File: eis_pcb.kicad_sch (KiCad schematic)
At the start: 69 parts, among them J1 527451897, J12 104031-0811, J2 GSB1C41110SSHR, J4 541020164, P1 V.BATT, P2 GND.BATT, Q3 IRLML6344TRPBF, SW1 SWT0210-045026GSA, SW2 SWT0210-045026GSA_REVA, U1 ESP32-S3-WROOM-1-N8R8, U2 AD5941BCPZ, U3 TMUX1109RSVR, U4 LSM6DSVTR, U5 BQ24075RGT, U6 NCP186AMX330TAG

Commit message: complete noise suppression, begin layout
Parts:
- removed SW1: SWT0210-045026GSA, SWT0210_045026GSA:SW_SWT0210-045026GSA_REVA, symbol SWT0210-045026GSA_REVA:SWT0210-045026GSA_REVA
- removed SW2: SWT0210-045026GSA_REVA, SWT0210_045026GSA:SW_SWT0210-045026GSA_REVA, symbol SWT0210-045026GSA_REVA:SWT0210-045026GSA_REVA
- added C15, C16, C36, C39, C41: 1u, Capacitor_SMD:C_0603_1608Metric, symbol Device:C_Small
- added C17, C32, C33, C35, C37, C38, C40: 100n, Capacitor_SMD:C_0402_1005Metric, symbol Device:C_Small
- added C34: 10u, Capacitor_SMD:C_0603_1608Metric, symbol Device:C_Small
- added FB1: 600R@100MHz, Diode_SMD:D_0805_2012Metric, symbol Device:FerriteBead_Small
- added R6, R7: 2.2R, Resistor_SMD:R_0402_1005Metric, symbol Device:R_Small_US
- added S1: PWR, SLW_864587_2A_RA_N_D:SW_SLW-864587-2A-RA-N-D, symbol SLW-864587-2A-RA-N-D:SLW-864587-2A-RA-N-D
- added SW1: RST, R_667995:R-667995_MIT, symbol Switch:SW_SPST
- added SW2: BOOT, R_667995:R-667995_MIT, symbol Switch:SW_SPST
- C11, C20, C5: footprint Capacitor_SMD:C_0402_1005Metric -> Capacitor_SMD:C_0603_1608Metric
- C12, C21, C26: value 0.1u -> 100n
- C13: value 0.1u -> 100n; footprint (none) -> Capacitor_SMD:C_0402_1005Metric
- C14: footprint (none) -> Capacitor_SMD:C_0402_1005Metric
- C18: value 10u -> 100n
- C19, C23: value 1u -> 100n
- C2: value 100n -> 1u; footprint Capacitor_SMD:C_0402_1005Metric -> Capacitor_SMD:C_0603_1608Metric
- C24: value 1u -> 22u; footprint Capacitor_SMD:C_0402_1005Metric -> Capacitor_SMD:C_0603_1608Metric
- C3: value 100n -> 10u; footprint Capacitor_SMD:C_0402_1005Metric -> Capacitor_SMD:C_0603_1608Metric
- C31: value 10u -> 100n; footprint Capacitor_SMD:C_0603_1608Metric -> Capacitor_SMD:C_0402_1005Metric
- J1: footprint CON_527451897_MOL -> 527451897:CON_527451897_MOL
- P1, P2: footprint (none) -> TestPoint:TestPoint_THTPad_D2.5mm_Drill1.2mm
- R3, R4, R5: footprint (none) -> Resistor_SMD:R_0402_1005Metric
- U1: footprint ESP32-S3-WROOM-1-N8R8:XCVR_ESP32S3WROOM1N8R8 -> RF_Module:ESP32-S3-WROOM-1
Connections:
- net +3V3: now also C16.1, C36.1, C37.1, C38.1, C40.1, C41.1, FB1.1, R7.2; no longer C1.1, C13.1, C2.1, C3.1, U2.30 (AVDD), U2.41 (AVDD), U2.6 (DVDD), U3.12 (VDD)
- net +5V: now also C33.2, C34.2
- net +VSYS: now also C35.1, S1.3; no longer C29.1, U5.10 (OUT), U5.11 (OUT)
- net BOOT: now also SW2.A
- net CS.AFE: no longer U1.31 (IO38)
- net CS.SCREEN: now also U1.18 (IO10); no longer R27.1, U1.32 (IO39)
- net CTP_INT: no longer J1.16
- net CTP_RST: no longer J1.15
- net GND: now also C15.2, C16.2, C17.2, C32.1, C33.1, C34.1, C35.2, C36.2, C37.2, C38.2, C39.2, C40.2, C41.2, SW1.B, SW2.B
- net MISO: no longer U1.30 (IO37)
- net MOSI: no longer J1.10, U1.28 (IO35)
- net PWR.EN: now also S1.2; no longer R5.1
- net SCLK: no longer J1.9, U1.29 (IO36)
- net SCREEN.RST: no longer J1.11
- net SW1: no longer U1.21 (IO13)
- net INT.IMU: now reaches U4.4 (INT1)
- net RST.SCREEN: now reaches U1.17 (IO9)
- net RST.SCREEN: now also J1.11
- net MOSI.SCREEN: now reaches U1.19 (IO11)
- net MOSI.SCREEN: now also J1.10
- net SCLK.SCREEN: now reaches U1.20 (IO12)
- net SCLK.SCREEN: now also J1.9
- net AFE.RST renamed RST.AFE
- net RST.AFE: no longer U1.18 (IO10)
- net CTP_SCL: no longer names the net of R29.1, U1.34 (IO41)
- net CTP_SCL: no longer J1.13
- net CTP_SDA: no longer names the net of R30.1, U1.35 (IO42)
- net CTP_SDA: no longer J1.14
- net DC renamed DC.SCREEN
- net DC.SCREEN: now also U1.21 (IO13); no longer U1.15 (IO3)
- net ESP.PWM: no longer names the net of U1.22 (IO14)
- net ESP.PWM: no longer R2.1
- net MCU.RST renamed RST.MCU
- net RST.MCU: now also SW1.A
- new net: C29.1, C32.2, U5.10 (OUT), U5.11 (OUT)
- new net: C1.1, C2.1, C3.1, R6.2, U2.30 (AVDD), U2.41 (AVDD)
- new net: C17.1, C39.1, R7.1, U2.6 (DVDD)
- new net: R27.1, U1.32 (IO39)
- new net: R5.1, S1.1
- new net 3V3A: C13.1, C15.1, FB1.2, R6.1, U3.12 (VDD)
- new net INT.TOUCH: J1.16
- new net PWM.SCREEN: R2.1
- new net RST.TOUCH: J1.15
- new net SCL.TOUCH: J1.13, U1.15 (IO3)
- new net SDA.TOUCH: J1.14
- no-connect marks 45 -> 44
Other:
- moved on the sheet: C1, C10, C12, C13, C19, C2, C20, C22, C23, C27, C28, C29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

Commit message: finish rev B schematic
did some layout planning
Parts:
- removed C14: 100n, Capacitor_SMD:C_0402_1005Metric, symbol Device:C_Small
- added C42: 100n, Capacitor_SMD:C_0402_1005Metric, symbol Device:C_Small
- added P3: DATA+, TestPoint:TestPoint_Pad_D2.0mm, symbol Connector:TestPoint
- added P4: DATA-, TestPoint:TestPoint_Pad_D2.0mm, symbol Connector:TestPoint
- added P5: RXD0, TestPoint:TestPoint_Pad_D2.0mm, symbol Connector:TestPoint
- added P6: TXD0, TestPoint:TestPoint_Pad_D2.0mm, symbol Connector:TestPoint
- added R32, R33, R34, R35, R36, R37, R38, R39, R40, R41: 10k, Resistor_SMD:R_0402_1005Metric, symbol Device:R_Small
- R1, R14, R16, R2, R25, R26, R27, R3, R4, R5, R6, R7: symbol Device:R_Small_US -> Device:R_Small
- R10, R11, R12, R13, R15, R17, R18, R19, R20, R9: symbol Device:R_US -> Device:R_Small
- R28, R29, R30, R31: value 4.7k -> 10k; symbol Device:R_Small_US -> Device:R_Small
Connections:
- net CTP_RST is gone; now on net CS.IMU: U1.24 (IO47)
- net SCREEN.RST is gone; now on net INT.IMU: U1.23 (IO21)
- net SW1 is gone; now on net GND: J12.9 (SW-1)
- net +3V3: now also R7.1, R32.2, R33.2, R34.2, R35.2, R36.2, R37.2; no longer R7.2
- net +5V: now also C34.1; no longer C34.2
- net +VSYS: now also C29.1, C32.2, U5.10 (OUT), U5.11 (OUT)
- net A0.MUX: now also U1.34 (IO41)
- net A1.MUX: now also U1.35 (IO42)
- net AVDD.REG: now also C4.1; no longer C8.1
- net BIAS.CAP: now also C8.1; no longer C7.1
- net CS.AFE: now also U1.31 (IO38), R35.1; no longer R26.1
- net CS.IMU: now also R36.1; no longer R31.1, U1.26 (IO45)
- net CS.SCREEN: now also R34.1
- net DATA+: now also P3.1
- net DATA-: now also P4.1
- net DVDD.1V8: now also C6.1; no longer C4.1
- net EN.MUX: now also U1.33 (IO40), R41.2
- net GND: now also C34.2, C42.2, R38.1, R39.1, R40.1, R41.1; no longer C34.1, J12.10 (SW-2)
- net INT.TOUCH: now also U1.11 (IO18), R37.1
- net K: now also R16.1; no longer R16.2
- net MISO: now also U1.10 (IO17); no longer J12.7 (DAT0)
- net MOSI: now also U1.9 (IO16); no longer J12.3 (CMD)
- net PWM.SCREEN: now also U1.22 (IO14)
- net REF.2V5: now also C7.1; no longer C6.1
- net RST.AFE: now also U1.32 (IO39), R40.2
- net RST.SCREEN: now also R39.2
- net RST.TOUCH: now also U1.12 (IO8), R38.2
- net SCL.TOUCH: now also R27.1
- net SCLK: now also U1.8 (IO15); no longer J12.5 (CLK)
- net SDA.TOUCH: now also R26.1, U1.38 (IO2)
- net V.BATT.SENSE: now also U1.4 (IO4), C42.1
- net at Q3.3: now also R16.2; no longer R16.1
- net at C17.1, C39.1, U2.6 (DVDD): now also R7.2; no longer R7.1
- net DAT2: now reaches J12.1 (DAT2)
- net DAT2: now also R31.1
- net DAT1: now reaches J12.8 (DAT1)
- net DAT1: now also R30.1
- net DAT0: now reaches R29.1
- net DAT0: now also J12.7 (DAT0), U1.5 (IO5); no longer U1.34 (IO41)
- net RXD0: now reaches U1.36 (RXD0)
- net RXD0: now also P5.1
- net TXD0: now reaches U1.37 (TXD0)
- net TXD0: now also P6.1
- net IO1: now reaches U1.39 (IO1)
- net CLK: now reaches U1.6 (IO6)
- net CLK: now also J12.5 (CLK)
- net CMD: now reaches U1.7 (IO7)
- net CMD: now also J12.3 (CMD), R28.1
- removed net CS.SD: J12.2 (CD/DAT3), R28.1, U1.33 (IO40)
- net CTP_INT renamed CD
- net CD: now also J12.10 (SW-2), R33.1
- new net DAT3: J12.2 (CD/DAT3), R32.1
- no-connect marks 44 -> 30
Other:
- note added: "Analog Front End"
- note added: "Power Switch"
- note removed: "AFE"
- company: (none) -> Liwei Lin Lab
- title: (none) -> Sweat Sensing EIS Mainboard
- moved on the sheet: C1, C10, C11, C12, C13, C15, C16, C17, C18, C19, C2, C20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

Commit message: remove redundant caps
removed some decoupling caps in power circuit because the components were so close together
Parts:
- removed C22: 1u, Capacitor_SMD:C_0603_1608Metric, symbol Device:C_Small
- removed C33, C35: 100n, Capacitor_SMD:C_0402_1005Metric, symbol Device:C_Small
- removed C34: 10u, Capacitor_SMD:C_0603_1608Metric, symbol Device:C_Small
- removed R25, R38: 10k, Resistor_SMD:R_0402_1005Metric, symbol Device:R_Small
- added P7: IO1, TestPoint:TestPoint_Pad_D2.0mm, symbol Connector:TestPoint
- C36: renamed from C19; footprint Capacitor_SMD:C_0603_1608Metric -> Capacitor_SMD:C_0402_1005Metric
- P1: value V.BATT -> +BATT; footprint TestPoint:TestPoint_THTPad_D2.5mm_Drill1.2mm -> TestPoint:TestPoint_THTPad_D2.0mm_Drill1.0mm
- P2: value GND.BATT -> GND; footprint TestPoint:TestPoint_THTPad_D2.5mm_Drill1.2mm -> TestPoint:TestPoint_THTPad_D2.0mm_Drill1.0mm
- renumbered C18 to C1, C40 to C10, C41 to C11, C4 to C12, C6 to C13, C5 to C14, C7 to C15, C8 to C16, C9 to C17, C10 to C18, C13 to C19, C23 to C2, C15 to C20, C26 to C21, C25 to C22, C12 to C23, C16 to C24, C11 to C25, C21 to C26, C36 to C27, C20 to C28, C37 to C29, C24 to C3, C38 to C30, C27 to C32, C32 to C33, C29 to C34, C28 to C35, C30 to C37, C42 to C4, C1 to C5, C2 to C6, C3 to C7, C17 to C8, C39 to C9, J4 to J1, J12 to J2, J1 to J3, J2 to J4, Q3 to Q1, R12 to R1, R40 to R10, R41 to R11, R1 to R12, R6 to R13, R7 to R14, R28 to R15, R29 to R16, R30 to R17, R31 to R18, R32 to R19, R17 to R2, R33 to R20, R16 to R21, R2 to R22, R14 to R23, R3 to R24, R4 to R25, R5 to R26, R20 to R27, R19 to R28, R18 to R29, R26 to R3, R11 to R30, R9 to R31, R10 to R32, R15 to R33, R13 to R34, R27 to R4, R34 to R5, R35 to R6, R36 to R7, R37 to R8, R39 to R9
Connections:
- net IO1: now also P7.1
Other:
- moved on the sheet: C36, C37, C4, J4, P3, P4, P5, P6, R26, R33, R34, S1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

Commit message: finish layout
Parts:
- removed C29: 100n, Capacitor_SMD:C_0402_1005Metric, symbol Device:C_Small
- P3, P4, P5, P6, P7: footprint TestPoint:TestPoint_Pad_D2.0mm -> TestPoint:TestPoint_Pad_D1.5mm
- renumbered C30 to C29, C31 to C30, C32 to C31, C33 to C32, C34 to C33, C35 to C34, C36 to C35, C37 to C36
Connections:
- net A1.MUX: now also U1.33 (IO40); no longer U1.35 (IO42)
- net CD: now also R15.1; no longer R20.1
- net CE1: now also J1.15; no longer J1.7
- net CE2: now also J1.16; no longer J1.8
- net CE3: now also J1.7; no longer J1.15
- net CE4: now also J1.8; no longer J1.16
- net CMD: now also R18.1; no longer R15.1
- net DAT0: now also R19.1; no longer R16.1
- net DAT1: now also R20.1; no longer R17.1
- net DAT2: now also R16.1; no longer R18.1
- net DAT3: now also R17.1; no longer R19.1
- net EN.MUX: now also U1.35 (IO42); no longer U1.33 (IO40)
- net GND: now also S1.SH1, S1.SH2
- net INT.IMU: now also U1.38 (IO2); no longer U1.23 (IO21)
- net SDA.TOUCH: now also U1.23 (IO21); no longer U1.38 (IO2)
- net WE1: now also J1.13; no longer J1.4
- net WE2: now also J1.12; no longer J1.5
- net WE3: now also J1.5; no longer J1.12
- net WE4: now also J1.4; no longer J1.13

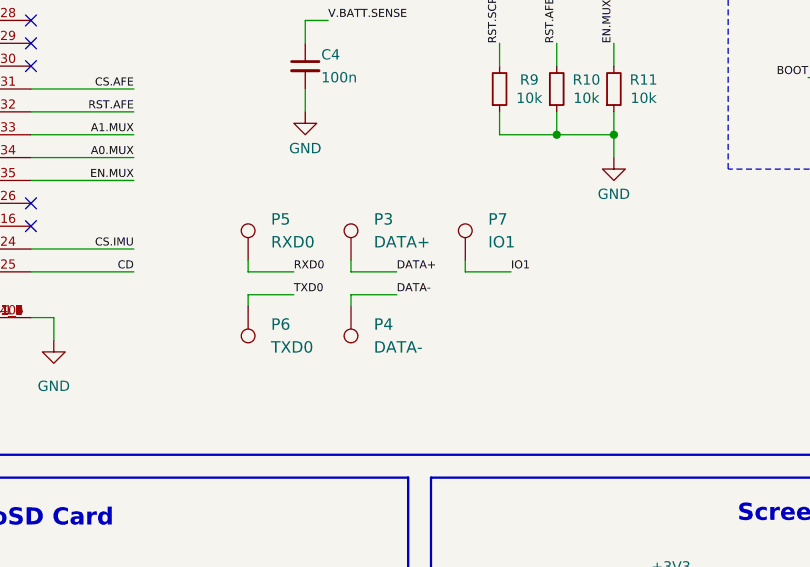
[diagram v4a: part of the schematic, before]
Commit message: fix drc/net errors, add via stitching
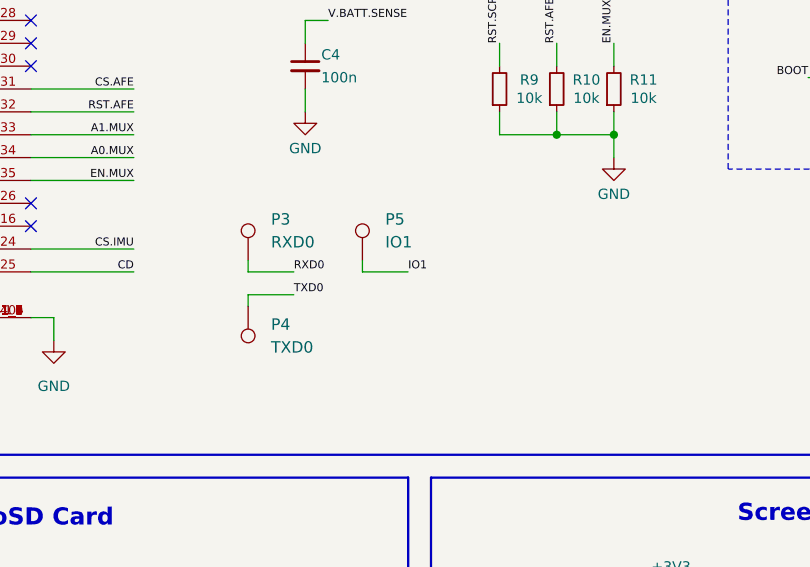
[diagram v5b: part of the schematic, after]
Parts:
- removed P3: DATA+, TestPoint:TestPoint_Pad_D1.5mm, symbol Connector:TestPoint
- removed P4: DATA-, TestPoint:TestPoint_Pad_D1.5mm, symbol Connector:TestPoint
- renumbered P5 to P3, P6 to P4, P7 to P5
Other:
- moved on the sheet: P5
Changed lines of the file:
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@@
 	(wire
 		(pts
-			(xy 303.53 91.44) (xy 308.61 91.44)
+			(xy 292.1 91.44) (xy 297.18 91.44)
 		)
 		(stroke
@@
 	(wire
 		(pts
-			(xy 290.83 90.17) (xy 290.83 91.44)
-		)
-		(stroke
-			(width 0)
-			(type default)
-		)
-	)
-	(wire
-		(pts
 			(xy 163.83 60.96) (xy 163.83 68.58)
 		)
@@
 	(wire
 		(pts
-			(xy 303.53 90.17) (xy 303.53 91.44)
+			(xy 292.1 90.17) (xy 292.1 91.44)
 		)
 		(stroke
@@
 	(wire
 		(pts
-			(xy 290.83 93.98) (xy 290.83 95.25)
-		)
-		(stroke
-			(width 0)
-			(type default)
-		)
-	)
-	(wire
-		(pts
 			(xy 87.63 49.53) (xy 90.17 49.53)
 		)
@@
 	(wire
 		(pts
-			(xy 290.83 91.44) (xy 295.91 91.44)
-		)
-		(stroke
-			(width 0)
-			(type default)
-		)
-	)
-	(wire
-		(pts
 			(xy 77.47 36.83) (xy 77.47 39.37)
 		)
@@
 	(wire
 		(pts
-			(xy 290.83 93.98) (xy 295.91 93.98)
-		)
-		(stroke
-			(width 0)
-			(type default)
-		)
-	)
-	(wire
-		(pts
 			(xy 213.36 55.88) (xy 224.79 55.88)
 		)
@@
 		)
 	)
-	(label "DATA-"
-		(at 295.91 93.98 0)
-		(effects
-			(font
-				(size 0.889 0.889)
-			)
-			(justify left bottom)
-		)
-	)
 	(label "RST.MCU"
 		(at 213.36 38.1 0)
@@
 	)
 	(label "IO1"
-		(at 308.61 91.44 0)
+		(at 297.18 91.44 0)
 		(effects
 			(font
@@
 		)
 	)
-	(label "DATA+"
-		(at 295.91 91.44 0)
-		(effects
-			(font
-				(size 0.889 0.889)
-			)
-			(justify left bottom)
-		)
-	)
 	(label "CE4"
 		(at 166.37 45.72 0)
@@
 		(dnp no)
 		(fields_autoplaced yes)
-		(property "Reference" "P6"
+		(property "Reference" "P4"
 			(at 281.94 97.2819 0)
 			(show_name no)
@@
 			(project "eis_pcb"
 				(path "/b9be45c7-595f-4fac-82ce-4faac3c4812a"
-					(reference "P6")
+					(reference "P4")
 					(unit 1)
 				)
@@
 	)
 	(symbol
-		(lib_id "Connector:TestPoint")
-		(at 290.83 90.17 0)
-		(unit 1)
-		(body_style 1)
-		(exclude_from_sim no)
-		(in_bom yes)
-		(on_board yes)
-		(in_pos_files yes)
-		(dnp no)
-		(fields_autoplaced yes)
-		(property "Reference" "P3"
-			(at 293.37 85.5979 0)
-			(show_name no)
-			(do_not_autoplace no)
-			(effects
-				(font
-					(size 1.27 1.27)
-				)
-				(justify left)
-			)
-		)
-		(property "Value" "DATA+"
-			(at 293.37 88.1379 0)
-			(show_name no)
-			(do_not_autoplace no)
-			(effects
-				(font
-					(size 1.27 1.27)
-				)
-				(justify left)
-			)
-		)
-		(property "Footprint" "TestPoint:TestPoint_Pad_D1.5mm"
-			(at 295.91 90.17 0)
-			(hide yes)
-			(show_name no)
-			(do_not_autoplace no)
-			(effects
-				(font
-					(size 1.27 1.27)
-				)
-			)
-		)
-		(property "Datasheet" ""
-			(at 295.91 90.17 0)
-			(hide yes)
-			(show_name no)
-			(do_not_autoplace no)
-			(effects
-				(font
-					(size 1.27 1.27)
-				)
-			)
-		)
-		(property "Description" "test point"
-			(at 290.83 90.17 0)
-			(hide yes)
-			(show_name no)
-			(do_not_autoplace no)
-			(effects
-				(font
-					(size 1.27 1.27)
-				)
-			)
-		)
-		(pin "1"
-		)
-		(instances
-			(project "eis_pcb"
-				(path "/b9be45c7-595f-4fac-82ce-4faac3c4812a"
-					(reference "P3")
-					(unit 1)
-				)
-			)
-		)
-	)
-	(symbol
 		(lib_id "Device:R_Small")
 		(at 320.04 71.12 0)
@@
 		(dnp no)
 		(fields_autoplaced yes)
-		(property "Reference" "P5"
+		(property "Reference" "P3"
 			(at 281.94 85.5979 0)
 			(show_name no)
@@
 			(project "eis_pcb"
 				(path "/b9be45c7-595f-4fac-82ce-4faac3c4812a"
-					(reference "P5")
+					(reference "P3")
 					(unit 1)
 				)
@@
 	)
 	(symbol
-		(lib_id "Connector:TestPoint")
-		(at 290.83 95.25 180)
-		(unit 1)
-		(body_style 1)
-		(exclude_from_sim no)
-		(in_bom yes)
-		(on_board yes)
-		(in_pos_files yes)
-		(dnp no)
-		(fields_autoplaced yes)
-		(property "Reference" "P4"
-			(at 293.37 97.2819 0)
-			(show_name no)
-			(do_not_autoplace no)
-			(effects
-				(font
-					(size 1.27 1.27)
-				)
-				(justify right)
-			)
-		)
-		(property "Value" "DATA-"
-			(at 293.37 99.8219 0)
-			(show_name no)
-			(do_not_autoplace no)
-			(effects
-				(font
-					(size 1.27 1.27)
-				)
-				(justify right)
-			)
-		)
-		(property "Footprint" "TestPoint:TestPoint_Pad_D1.5mm"
-			(at 285.75 95.25 0)
-			(hide yes)
-			(show_name no)
-			(do_not_autoplace no)
-			(effects
-				(font
-					(size 1.27 1.27)
-				)
-			)
-		)
-		(property "Datasheet" ""
-			(at 285.75 95.25 0)
-			(hide yes)
-			(show_name no)
-			(do_not_autoplace no)
-			(effects
-				(font
-					(size 1.27 1.27)
-				)
-			)
-		)
-		(property "Description" "test point"
-			(at 290.83 95.25 0)
-			(hide yes)
-			(show_name no)
-			(do_not_autoplace no)
-			(effects
-				(font
-					(size 1.27 1.27)
-				)
-			)
-		)
-		(pin "1"
-		)
-		(instances
-			(project "eis_pcb"
-				(path "/b9be45c7-595f-4fac-82ce-4faac3c4812a"
-					(reference "P4")
-					(unit 1)
-				)
-			)
-		)
-	)
-	(symbol
 		(lib_id "Device:R_Small")
 		(at 518.16 100.33 0)
@@
 	(symbol
 		(lib_id "Connector:TestPoint")
-		(at 303.53 90.17 0)
+		(at 292.1 90.17 0)
 		(unit 1)
 		(body_style 1)
@@
 		(dnp no)
 		(fields_autoplaced yes)
-		(property "Reference" "P7"
-			(at 306.07 85.5979 0)
+		(property "Reference" "P5"
+			(at 294.64 85.5979 0)
 			(show_name no)
 			(do_not_autoplace no)
@@
 		)
 		(property "Value" "IO1"
-			(at 306.07 88.1379 0)
+			(at 294.64 88.1379 0)
 			(show_name no)
 			(do_not_autoplace no)
@@
 		)
 		(property "Footprint" "TestPoint:TestPoint_Pad_D1.5mm"
-			(at 308.61 90.17 0)
+			(at 297.18 90.17 0)
 			(hide yes)
 			(show_name no)
@@
 		)
 		(property "Datasheet" ""
-			(at 308.61 90.17 0)
+			(at 297.18 90.17 0)
 			(hide yes)
 			(show_name no)
@@
 		)
 		(property "Description" "test point"
-			(at 303.53 90.17 0)
+			(at 292.1 90.17 0)
 			(hide yes)
 			(show_name no)
@@
 			(project "eis_pcb"
 				(path "/b9be45c7-595f-4fac-82ce-4faac3c4812a"
-					(reference "P7")
+					(reference "P5")
 					(unit 1)
 				)
